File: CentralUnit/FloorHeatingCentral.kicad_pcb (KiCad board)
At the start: 2 copper layers, 110 x 110 mm, 67 parts, among them J1 Screw_Terminal_01x02, J10 Screw_Terminal_01x02, J11 Screw_Terminal_01x02, J12 Screw_Terminal_01x02, J13 Screw_Terminal_01x02, J14 Screw_Terminal_01x04, J2 Conn_02x05_Odd_Even, J3 Conn_01x20, J4 Screw_Terminal_01x02, J5 Screw_Terminal_01x02, J6 Screw_Terminal_01x02, J7 Screw_Terminal_01x02, J8 Screw_Terminal_01x02, J9 Screw_Terminal_01x02, Q1 Q_NMOS_GDS, Q10 Q_NMOS_GDS, Q11 Q_NMOS_GDS, Q2 Q_NMOS_GDS, Q3 Q_NMOS_GDS, Q4 Q_NMOS_GDS, Q5 Q_NMOS_GDS, Q6 Q_NMOS_GDS, Q7 Q_NMOS_GDS, Q8 Q_NMOS_GDS, Q9 Q_NMOS_GDS, U1 ESP32-DevKitC, U2 74HC595D_118, U3 74HC595D_118, U4 RFM69-ATSHA-breakout, U5 MP1584, U6 LM1117-5.0

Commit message: Minor changes
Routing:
- net +3V3: track 346.3 -> 342.0 mm
- net Net-(J3-Pad3): track 47.4 -> 46.3 mm
- net +7.5V: vias 2 -> 1
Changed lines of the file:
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@@
   (segment (start 119.099991 89.896369) (end 112 82.796378) (width 1) (layer "F.Cu") (net 1))
   (via (at 119.4 109) (size 0.8) (drill 0.4) (layers "F.Cu" "B.Cu") (net 1))
-  (via (at 126.9 109.1) (size 0.8) (drill 0.4) (layers "F.Cu" "B.Cu") (net 1))
-  (segment (start 162.4058 117.898541) (end 157.203629 112.696371) (width 1) (layer "B.Cu") (net 1))
+  (segment (start 156.582831 112.075573) (end 162.4058 117.898541) (width 1) (layer "B.Cu") (net 1))
   (segment (start 193.7 117.2) (end 193.001459 117.898541) (width 1) (layer "B.Cu") (net 1))
-  (segment (start 156.582831 112.075573) (end 154.7 112.075573) (width 1) (layer "B.Cu") (net 1))
-  (segment (start 154.7 112.075573) (end 122.475573 112.075573) (width 1) (layer "B.Cu") (net 1))
+  (segment (start 122.475573 112.075573) (end 156.582831 112.075573) (width 1) (layer "B.Cu") (net 1))
   (segment (start 193.001459 117.898541) (end 162.4058 117.898541) (width 1) (layer "B.Cu") (net 1))
   (segment (start 122.475573 112.075573) (end 119.4 109) (width 1) (layer "B.Cu") (net 1))
-  (segment (start 157.203629 112.696371) (end 156.582831 112.075573) (width 1) (layer "B.Cu") (net 1))
   (segment (start 90.520489 122.839511) (end 90.8 122.56) (width 1) (layer "F.Cu") (net 2))
   (segment (start 106.434755 153.915244) (end 106.434755 155.189244) (width 1) (layer "F.Cu") (net 2))
@@
   (segment (start 180.858489 62.484) (end 182.88 64.505511) (width 0.25) (layer "F.Cu") (net 3))
   (segment (start 157.988 128.778) (end 157.193 128.778) (width 0.25) (layer "F.Cu") (net 3))
-  (segment (start 127.25768 61.460231) (end 130.563769 61.460231) (width 0.25) (layer "F.Cu") (net 3))
   (segment (start 143.257408 124.206) (end 144.732408 125.681) (width 0.25) (layer "F.Cu") (net 3))
   (segment (start 144.732408 125.681) (end 146.05 125.681) (width 0.25) (layer "F.Cu") (net 3))
@@
   (segment (start 134.985 122.985) (end 135.255 123.255) (width 0.25) (layer "F.Cu") (net 3))
   (segment (start 158 128.79) (end 157.988 128.778) (width 0.25) (layer "F.Cu") (net 3))
-  (segment (start 130.755711 61.652173) (end 130.563769 61.460231) (width 0.25) (layer "F.Cu") (net 3))
   (segment (start 148.033 125.681) (end 146.05 125.681) (width 0.25) (layer "F.Cu") (net 3))
   (segment (start 150.584501 125.513499) (end 155.231499 125.513499) (width 0.25) (layer "F.Cu") (net 3))
-  (segment (start 130.563769 61.460231) (end 131.056231 61.460231) (width 0.25) (layer "F.Cu") (net 3))
   (segment (start 157.193 128.778) (end 156.845 128.43) (width 0.25) (layer "F.Cu") (net 3))
   (segment (start 135.289998 123.289998) (end 135.255 123.255) (width 0.25) (layer "F.Cu") (net 3))
@@
   (segment (start 158 138) (end 158.724501 137.275499) (width 0.25) (layer "B.Cu") (net 3))
   (segment (start 135.923998 124.206) (end 135.289998 124.84) (width 0.25) (layer "B.Cu") (net 3))
-  (segment (start 135.163998 124.714) (end 135.289998 124.84) (width 0.25) (layer "B.Cu") (net 3))
   (segment (start 116 127.5) (end 115.5 128) (width 0.25) (layer "B.Cu") (net 3))
   (segment (start 99.748 113.21) (end 136.29 113.21) (width 0.25) (layer "B.Cu") (net 3))
@@
   (segment (start 157.48 74.665511) (end 152.90528 79.240231) (width 0.25) (layer "B.Cu") (net 55))
   (segment (start 152.90528 79.240231) (end 152.65768 79.240231) (width 0.25) (layer "B.Cu") (net 55))
+  (segment (start 147.353501 142.895305) (end 146.665489 142.207293) (width 0.25) (layer "F.Cu") (net 60))
+  (segment (start 144.78 127) (end 144.234501 126.454501) (width 0.25) (layer "F.Cu") (net 60))
+  (segment (start 139.710489 64.495022) (end 140.208 63.997511) (width 0.25) (layer "F.Cu") (net 60))
+  (segment (start 140.161901 126.454501) (end 139.710489 126.003089) (width 0.25) (layer "F.Cu") (net 60))
+  (segment (start 139.710489 126.003089) (end 139.710489 64.495022) (width 0.25) (layer "F.Cu") (net 60))
   (segment (start 144.769511 127.010489) (end 144.78 127) (width 0.25) (layer "F.Cu") (net 60))
+  (segment (start 149.205489 142.895305) (end 147.353501 142.895305) (width 0.25) (layer "F.Cu") (net 60))
+  (segment (start 146.665489 142.207293) (end 146.665489 141.425273) (width 0.25) (layer "F.Cu") (net 60))
+  (segment (start 137.795 121.7844) (end 139.241889 120.337511) (width 0.25) (layer "F.Cu") (net 60))
+  (segment (start 150.38 141.720794) (end 149.205489 142.895305) (width 0.25) (layer "F.Cu") (net 60))
   (segment (start 144.769511 139.529295) (end 144.769511 127.010489) (width 0.25) (layer "F.Cu") (net 60))
+  (segment (start 137.795 123.03) (end 137.795 121.7844) (width 0.25) (layer "F.Cu") (net 60))
+  (segment (start 144.234501 126.454501) (end 140.161901 126.454501) (width 0.25) (layer "F.Cu") (net 60))
+  (segment (start 139.241889 120.337511) (end 139.583467 120.337511) (width 0.25) (layer "F.Cu") (net 60))
   (segment (start 146.665489 141.425273) (end 144.769511 139.529295) (width 0.25) (layer "F.Cu") (net 60))
-  (segment (start 144.78 127) (end 144.234501 126.454501) (width 0.25) (layer "F.Cu") (net 60))
-  (segment (start 146.665489 142.207293) (end 146.665489 141.425273) (width 0.25) (layer "F.Cu") (net 60))
-  (segment (start 147.353501 142.895305) (end 146.665489 142.207293) (width 0.25) (layer "F.Cu") (net 60))
-  (segment (start 139.710489 126.003089) (end 139.710489 120.639511) (width 0.25) (layer "F.Cu") (net 60))
-  (segment (start 137.795 121.7844) (end 139.241889 120.337511) (width 0.25) (layer "F.Cu") (net 60))
-  (segment (start 140.208 63.997511) (end 140.012489 64.193022) (width 0.25) (layer "F.Cu") (net 60))
-  (segment (start 137.795 123.03) (end 137.795 121.7844) (width 0.25) (layer "F.Cu") (net 60))
-  (segment (start 149.205489 142.895305) (end 147.353501 142.895305) (width 0.25) (layer "F.Cu") (net 60))
-  (segment (start 139.241889 120.337511) (end 139.583467 120.337511) (width 0.25) (layer "F.Cu") (net 60))
-  (segment (start 144.234501 126.454501) (end 140.161901 126.454501) (width 0.25) (layer "F.Cu") (net 60))
-  (segment (start 139.710489 64.495022) (end 140.208 63.997511) (width 0.25) (layer "F.Cu") (net 60))
-  (segment (start 139.710489 120.639511) (end 139.710489 120.210489) (width 0.25) (layer "F.Cu") (net 60))
-  (segment (start 139.710489 120.210489) (end 139.710489 64.495022) (width 0.25) (layer "F.Cu") (net 60))
-  (segment (start 140.161901 126.454501) (end 139.710489 126.003089) (width 0.25) (layer "F.Cu") (net 60))
-  (segment (start 150.38 141.720794) (end 149.205489 142.895305) (width 0.25) (layer "F.Cu") (net 60))
   (via (at 140.208 63.997511) (size 0.8) (drill 0.4) (layers "F.Cu" "B.Cu") (net 60))
   (segment (start 159.453511 75.232) (end 159.453511 72.562462) (width 0.25) (layer "B.Cu") (net 60))
   (segment (start 157.930049 71.039) (end 157.029951 71.039) (width 0.25) (layer "B.Cu") (net 60))
+  (segment (start 140.708231 64.000231) (end 152.65768 64.000231) (width 0.25) (layer "B.Cu") (net 60))
   (segment (start 155.194 69.203049) (end 155.194 66.536551) (width 0.25) (layer "B.Cu") (net 60))
+  (segment (start 140.708231 64.000231) (end 140.21072 64.000231) (width 0.25) (layer "B.Cu") (net 60))
   (segment (start 157.48 77.205511) (end 159.453511 75.232) (width 0.25) (layer "B.Cu") (net 60))
   (segment (start 140.208 63.997511) (end 140.21072 64.000231) (width 0.25) (layer "B.Cu") (net 60))
@@
   (segment (start 155.194 66.536551) (end 152.65768 64.000231) (width 0.25) (layer "B.Cu") (net 60))
   (segment (start 157.029951 71.039) (end 155.194 69.203049) (width 0.25) (layer "B.Cu") (net 60))
-  (segment (start 140.21072 64.000231) (end 152.65768 64.000231) (width 0.25) (layer "B.Cu") (net 60))
   (segment (start 145.22951 126.813806) (end 144.420694 126.00499) (width 0.25) (layer "F.Cu") (net 61))
   (segment (start 147.84 130.400978) (end 148.999022 130.400978) (width 0.25) (layer "F.Cu") (net 61))
@@
   (segment (start 141.605 123.631072) (end 141.605 123.03) (width 0.25) (layer "F.Cu") (net 61))
   (segment (start 143.978918 126.00499) (end 141.605 123.631072) (width 0.25) (layer "F.Cu") (net 61))
-  (segment (start 192.4 142.8) (end 195.015 145.415) (width 0.25) (layer "F.Cu") (net 72))
-  (segment (start 196 145.415) (end 195.155 145.415) (width 0.25) (layer "F.Cu") (net 72))
-  (segment (start 195.015 145.415) (end 196 145.415) (width 0.25) (layer "F.Cu") (net 72))
-  (segment (start 191.4 139.4) (end 190 138) (width 0.25) (layer "F.Cu") (net 72))
-  (segment (start 192.4 140.4) (end 192.4 142.8) (width 0.25) (layer "F.Cu") (net 72))
-  (segment (start 191.4 139.4) (end 192.4 140.4) (width 0.25) (layer "F.Cu") (net 72))
+  (segment (start 190 138) (end 192.540489 140.540489) (width 0.25) (layer "F.Cu") (net 72))
+  (segment (start 195.453 145.415) (end 196 145.415) (width 0.25) (layer "F.Cu") (net 72))
+  (segment (start 192.540489 142.502489) (end 195.453 145.415) (width 0.25) (layer "F.Cu") (net 72))
+  (segment (start 192.540489 140.540489) (end 192.540489 142.502489) (width 0.25) (layer "F.Cu") (net 72))
   (via (at 190 138) (size 0.8) (drill 0.4) (layers "F.Cu" "B.Cu") (net 72))
   (segment (start 190 138) (end 159.180794 138) (width 0.25) (layer "B.Cu") (net 72))

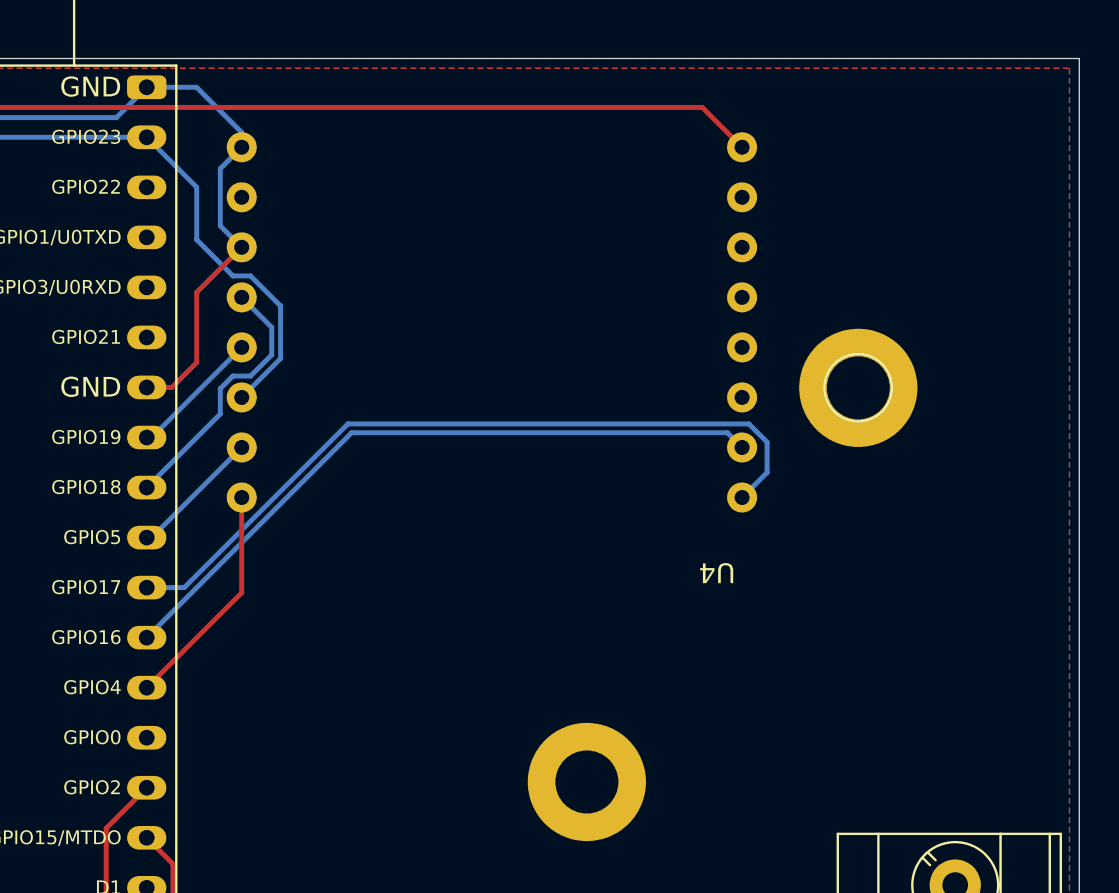
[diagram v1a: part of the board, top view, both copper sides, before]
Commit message: Added I2c ports. Final routing. Production.
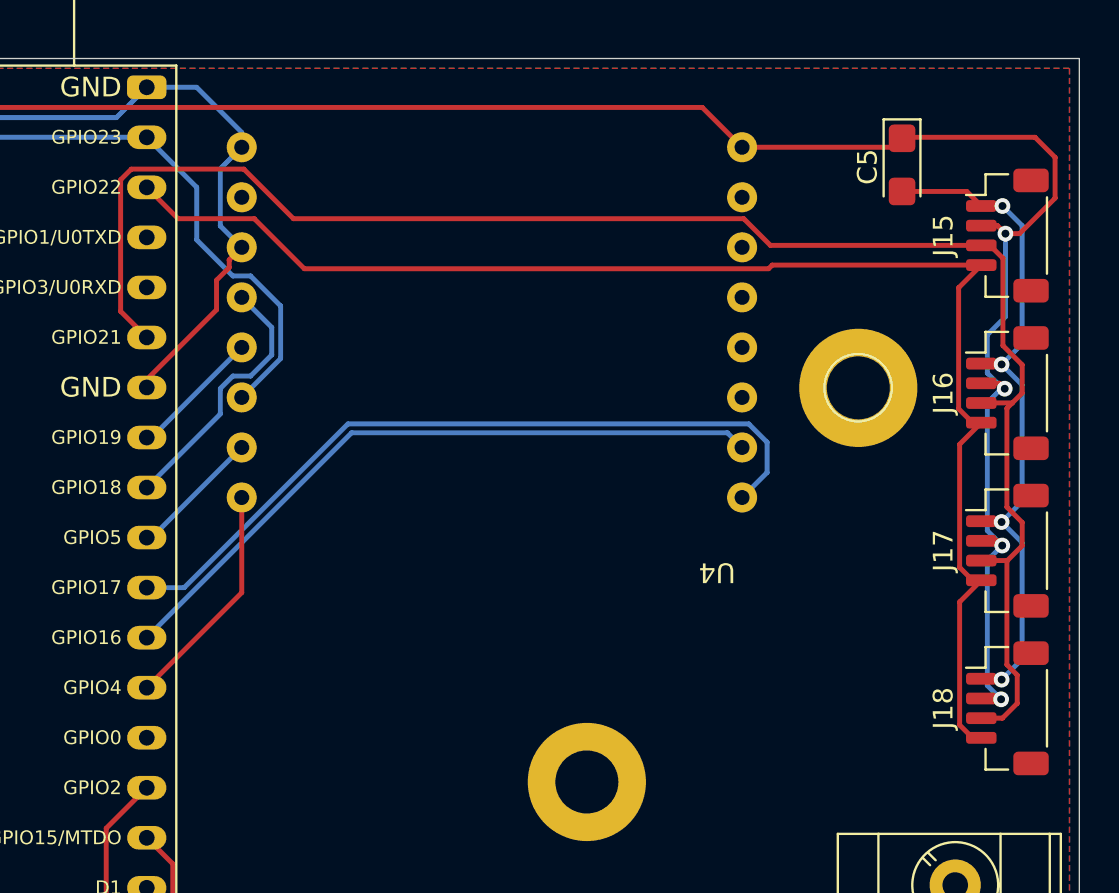
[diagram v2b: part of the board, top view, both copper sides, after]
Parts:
- added C5: 10u, Capacitor_Tantalum_SMD:CP_EIA-3216-18_Kemet-A, F.Cu at (191.0, 65.4)
- added J15: Conn_01x04_Male, Connector_JST:JST_SH_BM04B-SRSS-TB_1x04-1MP_P1.00mm_Vertical, F.Cu at (196.3, 69.0)
- added J16: Conn_01x04_Male, Connector_JST:JST_SH_BM04B-SRSS-TB_1x04-1MP_P1.00mm_Vertical, F.Cu at (196.3, 77.0)
- added J17: Conn_01x04_Male, Connector_JST:JST_SH_BM04B-SRSS-TB_1x04-1MP_P1.00mm_Vertical, F.Cu at (196.3, 85.0)
- added J18: Conn_01x04_Male, Connector_JST:JST_SH_BM04B-SRSS-TB_1x04-1MP_P1.00mm_Vertical, F.Cu at (196.3, 93.0)
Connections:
- U1 pad 33: unconnected-(U1-Pad33) -> /SDA
- U1 pad 36: unconnected-(U1-Pad36) -> /SCL
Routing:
- net /SDA: track 0.00 -> 84.7 mm
- net /SCL: track 0.00 -> 71.7 mm
- net +3V3: track 342.0 -> 394.6 mm, vias 7 -> 11
- net GND: track 530.0 -> 564.5 mm, vias 8 -> 12
